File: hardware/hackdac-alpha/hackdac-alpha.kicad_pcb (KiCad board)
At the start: 4 copper layers, 120 x 75 mm, 222 parts, among them J1 VIDEO OUT, J10 HOLE, J11 HOLE, J12 EXT POWER, J13 TTL SYNC, J2 SYNC OUT, J3 I2C, J4 AUDIO OUT, J5 EXT 5V, J6 HOLE, J7 HOLE, J8 HOLE, J9 HOLE, P1 BANK2_AUX, P2 P22, P3 P20, P4 P28, Q1 2N7002, Q2 BC857, Q3 BC857, Q4 2N7002, Q5 2N7002, Q6 IRLML2244, U1 AD768, U10 KF50BDT, U11 L78L05_SO8, U12 L79L05_SO8, U13 LM66200, U14 TPS61170DRVR, U15 TPS63700DRCT, U2 MAX4104, U3 TLE2082, U4 MAX4104, U5 MCP47FEB22A1-E/ST, U6 74LVCH16T245, U7 74LVC1T45, U8 MCP1700T-3302E/MB, U9 PCM5102, X1 ECS-TXO-3225-270-TR

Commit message: Update with V2 mods
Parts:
- added REF**: SOT-23, Package_TO_SOT_SMD:SOT-23, F.Cu at (137.1, 107.7)
- added REF**: R_0603_1608Metric, Resistor_SMD:R_0603_1608Metric, F.Cu at (146.0, 118.3)
- added REF**: R_0603_1608Metric, Resistor_SMD:R_0603_1608Metric, F.Cu at (134.9, 108.9)
- added U16: 74LVC1G125, Package_TO_SOT_SMD:SOT-23-5, F.Cu at (148.2, 120.8)
- L11: value L -> 5u6
- R21: value 1k8 -> 750
- R24: value 270 -> 487
- R36: value 1k8 -> 1k5
- R53, R54: value R -> 100
- R57: value NF -> 0
- R60: value 55k6 -> 30k9
- R63: value 988k -> 619k
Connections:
- P2 pad 2: unconnected-(P2-Pin_2-Pad2) -> TCXO_CLK
- P4 pad 15: TCXO_CLK -> unconnected-(P4-Pin_15-Pad15)
- P4 pad 3: unconnected-(P4-Pin_3-Pad3) -> TCXO_ENABLE
- R32 pad 2: TCXO_CLK -> Net-(R32-Pad2)
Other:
- board text added: "REWORK WIRE LENGTHS: TCXO_CLK: 51MM U16 IN: 19MM GND: 9MM"

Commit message: V3 PCB WIP
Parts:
- removed the C54 at (158.4, 79.8)
- removed the C68 at (183.3, 82.5)
- removed the C69 at (160.7, 93.7)
- removed the C71 at (183.3, 86.6)
- removed the C72 at (151.8, 96.1)
- removed the C73 at (151.8, 99.9)
- removed the C74 at (137.4, 94.8)
- removed the C75 at (137.4, 100.0)
- removed C79: 100n, Capacitor_SMD:C_0603_1608Metric
- removed the D5 at (182.5, 77.5)
- removed the J5 at (185.9, 75.8)
- removed the L11 at (123.6, 126.9)
- removed the L12 at (164.8, 96.5)
- removed the L13 at (164.8, 100.0)
- removed L16: NF, Inductor_SMD:L_1210_3225Metric
- removed L17: 5u6, Inductor_SMD:L_1210_3225Metric
- removed the R45 at (108.8, 129.9)
- removed the R46 at (108.8, 131.6)
- removed the R47 at (108.8, 133.2)
- removed the R48 at (108.8, 134.9)
- removed the R55 at (157.5, 95.7)
- removed the R56 at (157.5, 102.3)
- removed the R57 at (182.8, 94.4)
- removed REF**: SOT-23, Package_TO_SOT_SMD:SOT-23
- removed REF** (x2): R_0603_1608Metric, Resistor_SMD:R_0603_1608Metric
- removed the U11 at (157.5, 97.6)
- removed the U12 at (157.5, 103.3)
- removed U13: LM66200, Package_TO_SOT_SMD:SOT-583-8
- removed U16: 74LVC1G125, Package_TO_SOT_SMD:SOT-23-5
- added D7: RF OUT, LED_SMD:LED_0805_2012Metric, F.Cu at (220.7, 78.9)
- added J6: EXT LEDS, Connector_Molex:Molex_PicoBlade_53047-0410_1x04_P1.25mm_Vertical, F.Cu at (233.3, 77.3)
- added Q2: BC847, Package_TO_SOT_SMD:SOT-23, F.Cu at (208.9, 79.8)
- added R50: 100, Resistor_SMD:R_0603_1608Metric, F.Cu at (220.5, 81.7)
- added R51: 100, Resistor_SMD:R_0603_1608Metric, F.Cu at (228.7, 78.0)
- added R52: 100, Resistor_SMD:R_0603_1608Metric, F.Cu at (228.7, 80.5)
- added R54: 10k, Resistor_SMD:R_0603_1608Metric, F.Cu at (228.7, 83.1)
- C10: value 1n -> 1n5
- C11: value 560p -> NF
- C12, C17, C18, C29: value 100p -> NF
- C13: value 82p -> NF
- C14: value 100p -> 270p
- C15: value 680p -> 3n9
- C16: value 2n2 -> NF
- C19: value 100p -> 300p
- C20: value 1n -> NF
- C21: renamed from C22; value 82p -> 300p
- C22: renamed from C21; value 220p -> NF
- C24: renamed from C25; value 220p -> 620p
- C25: renamed from C24; value 390p -> NF
- C26: renamed from C27; value 270p -> NF
- C27: renamed from C26; value NF -> 270p
- C28: value 560p -> 680p
- C30: value 18p -> NF
- C31: value 220p -> 240p
- C36: value 47p -> 47pF
- C40: renamed from C41; value 560p -> 1n
- C41: renamed from C40; value 390p -> NF
- R13, R20: value 100 -> NF
- R14, R18: value 100 -> 50
- R21: value 750 -> 470
- R22: renamed from R23; value 180 -> 169
- R23: renamed from R22; value 3k3 -> NF
- R24: value 487 -> 330
- R25: value 330 -> 220
- R26: value 100 -> 75
- R32: renamed from R39; value 100 -> 39
- R33: value 10 -> 10k
- R34: renamed from R31; value NF -> 10k
- R36: renamed from R32; value 100 -> 39
- R49: value 0 -> 100
- U10: value KF50BDT -> 74LVC1G07; footprint Package_TO_SOT_SMD:TO-252-2 -> Package_TO_SOT_SMD:SOT-23-5
- U7: value 74LVC1T45 -> 74LVC1G125; footprint Package_TO_SOT_SMD:SOT-23-6 -> Package_TO_SOT_SMD:SOT-23-5
- moved R49 130.9 mm to (228.7, 75.5), turned to 0 degrees
- moved R33 93.6 mm to (228.7, 87.6), turned to 0 degrees
- moved Q1 82.2 mm to (208.9, 84.4), turned to 0 degrees
- moved C70 52.3 mm to (121.2, 71.4)
- moved C48 36.4 mm to (168.8, 109.3), turned to -90 degrees
- moved U7 32.9 mm to (165.8, 109.2), turned to 0 degrees
- moved C69 29.1 mm to (130.0, 65.3), turned to 0 degrees
- moved C65 19.3 mm to (148.9, 96.8), turned to -90 degrees
- moved C66 17.9 mm to (150.6, 96.8)
- moved R36 15.8 mm to (162.8, 109.3), turned to -90 degrees
- moved U10 14.5 mm to (181.2, 95.2)
- moved X1 11.8 mm to (159.7, 109.2), turned to 90 degrees
- moved C47 11.4 mm to (156.7, 109.3), turned to -90 degrees
- moved L12 11.4 mm to (137.2, 98.4)
- moved L11 11.3 mm to (137.2, 95.0)
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- renumbered C46 to C45, C47 to C46, C45 to C47, C55 to C54, C56 to C55, C57 to C56, C58 to C57, C59 to C58, C60 to C59, C61 to C60, C62 to C61, C63 to C62, C64 to C63, C65 to C64, C66 to C65, C67 to C66, C76 to C67, C77 to C68, C78 to C69, C80 to C71, C81 to C72, C82 to C73, C83 to C74, C84 to C75, C85 to C76, C86 to C77, C87 to C78, D6 to D5, D7 to D6, J8 to J10, J9 to J11, J10 to J12, J11 to J13, J13 to J2, J2 to J3, J3 to J4, J4 to J5, J12 to J7, J6 to J8, J7 to J9, L14 to L11, L15 to L12, L18 to L13, L19 to L14, P4 to P3, P3 to P4, Q2 to Q3, Q3 to Q4, Q4 to Q5, Q5 to Q6, Q6 to Q7, R35 to R31, R34 to R35, R36 to R37, R37 to R38, R38 to R39, R50 to R45, R51 to R46, R52 to R47, R53 to R48, R54 to R53, R58 to R55, R59 to R56, R60 to R57, R61 to R58, R62 to R59, R63 to R60, U14 to U11, U15 to U12
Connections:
- C45 pad 1: VCC -> +5V
- C46 pad 1: VCC -> +5V
- C53 pad 2: -VDAC -> -5VA
- C54 pad 1: Net-(U8-VI) -> VIN
- C63 pad 1: Net-(J4-IN2) -> Net-(J5-IN2)
- C64 pad 1: Net-(J4-IN1) -> Net-(J5-IN1)
- C65 pad 1: +VDAC -> +5V
- C66 pad 2: -VDAC -> -5V
- C70 pad 2: Net-(C70-Pad2) -> -5VA
- C76 pad 1: +VDAC -> +5V
- C77 pad 1: -VDAC -> -5V
- D4 pad 1: -VDAC -> -5VA
- D5 pad 1: GND -> Net-(D5-K)
- D5 pad 2: Net-(D6-A) -> +3.3V_HACKRF
- D6 pad 1: Net-(D7-K) -> Net-(D6-K)
- D8 pad 1: +VDAC -> +5V
- D9 pad 2: -VDAC -> -5V
- J5 pad 1: Net-(J4-IN1) -> Net-(J5-IN1)
- J5 pad 2: Net-(J4-IN2) -> Net-(J5-IN2)
- J7 pad 1: +VDAC -> -5V
- J7 pad 3: -VDAC -> +5V
- P1 pad 17: /video-misc/LAD0 -> unconnected-(P1-Pin_17-Pad17)
- P2 pad 22: unconnected-(P2-Pin_22-Pad22) -> PWR_EN
- P3 pad 7: unconnected-(P4-Pin_7-Pad7) (its old number) -> /power/RF_OUT_LED
- P4 pad 13: unconnected-(P3-Pin_13-Pad13) (its old number) -> GND
- P4 pad 15: unconnected-(P3-Pin_15-Pad15) (its old number) -> GND
- P4 pad 17: /power/VBUSCTRL -> unconnected-(P4-Pin_17-Pad17)
- P4 pad 19: unconnected-(P3-Pin_19-Pad19) (its old number) -> GND
- Q1 pad 1: Net-(Q1-G) -> LSYNC
- Q3 pad 2: Net-(Q1-D) -> Net-(Q2-C)
- Q4 pad 3: -VDAC -> -5VA
- Q7 pad 1: /power/VBUSCTRL -> Net-(Q7-G)
- Q7 pad 3: Net-(Q6-D) -> VIN
- R31 pad 2: Net-(U7-A) -> Net-(U6-1A1)
- R32 pad 1: Net-(U7-B) -> Net-(U6-1B1)
- R33 pad 1: LSYNC -> +5VA
- R33 pad 2: Net-(Q1-G) -> Net-(Q1-D)
- R35 pad 2: Net-(Q1-D) -> Net-(Q2-C)
- R36 pad 2: Net-(R32-Pad2) -> Net-(R36-Pad2)
- R46 pad 2: Net-(J4-IN1) -> Net-(J5-IN2)
- R47 pad 2: Net-(J4-IN2) -> Net-(J5-IN1)
- R48 pad 1: +3.3V_HACKRF -> Net-(D5-K)
- R48 pad 2: Net-(D6-A) -> GND
- R49 pad 2: Net-(U9-SCK) -> Net-(J6-Pin_2)
- R53 pad 1: /power/VIDEO_OUT_LED -> /power/RF_OUT_LED
- R57 pad 1: +VDAC -> +5V
- R60 pad 2: -VDAC -> -5V
- U1 pad 7: AD0 -> GND
- U10 pad 1: Net-(D5-K) -> (no net)
- U10 pad 2: GND -> PWR_EN
- U10 pad 3: Net-(U10-VO) -> GND
- U12 pad 8: -VDAC -> -5V
- U6 pad 18: VCC -> +5V
- U6 pad 2: AD0 -> Net-(U6-1B1)
- U6 pad 47: /video-misc/LAD0 -> Net-(U6-1A1)
- U6 pad 7: VCC -> +5V
- U7 pad 1: +3.3V_HACKRF -> TCXO_ENABLE
- U7 pad 2: GND -> Net-(R36-Pad2)
- U7 pad 3: Net-(U7-A) -> GND
- U7 pad 4: Net-(U7-B) -> TCXO_CLK
- U8 pad 2: Net-(U8-VI) -> VIN
- U9 pad 12: Net-(U9-SCK) -> GND
- U9 pad 13: Net-(U9-BCK) -> /audio/I2S_SCK
- U9 pad 14: Net-(U9-DIN) -> /audio/I2S_SDA
- U9 pad 15: Net-(U9-LRCK) -> /audio/I2S_WS
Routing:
- net GND: track 1209.2 -> 1031.0 mm, vias 174 -> 133
- net -VDAC: track 106.5 -> 0.00 mm, vias 12 -> 0
- net +VDAC: track 60.6 -> 0.00 mm, vias 12 -> 0
- net (no net): track 0.00 -> 57.1 mm
- net PWR_EN: track 0.00 -> 45.0 mm, vias 0 -> 1
- net VCC: track 44.0 -> 0.00 mm, vias 6 -> 0
- net Net-(J4-IN2): track 37.4 -> 0.00 mm
- net AD0: track 32.4 -> 0.00 mm, vias 2 -> 0
- net TCXO_CLK: track 10.5 -> 40.8 mm, vias 0 -> 1
- net +3.3V_HACKRF: track 250.9 -> 279.1 mm, vias 11 -> 8
- net TCXO_ENABLE: track 0.00 -> 27.4 mm, vias 0 -> 1
- net Net-(U8-VI): track 22.7 -> 0.00 mm, vias 11 -> 0
- net VIN: track 157.7 -> 136.8 mm, vias 13 -> 14
- net Net-(J4-IN1): track 18.0 -> 0.00 mm
- net Net-(C70-Pad2): track 18.0 -> 0.00 mm
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- added copper zone on In1.Cu, net +5V
- added copper zone on F.Cu, net -5V
- removed copper zone on F.Cu, net +VDAC
- removed copper zone on In1.Cu, net +VDAC
- removed copper zone on F.Cu, net -VDAC
- removed copper zone on In1.Cu, net -VDAC
- removed copper zone on F.Cu, net Net-(Q6-D)
- removed copper zone on F.Cu, net Net-(U10-VO)
- removed copper zone on In1.Cu, net Net-(U8-VI)
- removed copper zone on In1.Cu, net VCC
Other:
- board text added: "HackDAC Alpha v3"
- board text removed: "+12V IN"
- board text removed: "HackDAC Alpha v2"
- board text removed: "REWORK WIRE LENGTHS: TCXO_CLK: 51MM U16 IN: 19MM GND: 9MM"

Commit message: V3 PCB WIP
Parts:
- moved D7 126.6 mm to (100.0, 116.9), turned to 180 degrees
- moved R49 121.4 mm to (103.5, 114.1), turned to 180 degrees
- moved R33 92.8 mm to (137.5, 104.6)
- moved J6 86.9 mm to (149.9, 101.7)
- moved Q2 83.9 mm to (131.8, 113.1)
- moved Q1 75.8 mm to (137.2, 108.9)
- moved R53 45.6 mm to (184.0, 91.5)
- moved R48 5.34 mm to (103.5, 111.4), turned to 0 degrees
- moved D5 5.33 mm to (100.0, 111.4), turned to 180 degrees
- moved C63 5.25 mm to (94.6, 126.7)
- moved C64 5.16 mm to (94.6, 131.9)
- moved R50 2.80 mm to (103.5, 116.9)
- turned D6 to 180 degrees
- renumbered R50 to R49, R53 to R50, R49 to R51, R51 to R52, R54 to R53, R52 to R54
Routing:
- net (no net): track 57.1 -> 0.00 mm
- net /power/RF_OUT_LED: track 0.00 -> 47.8 mm
- net Net-(J5-IN2): track 0.00 -> 33.1 mm
- net Net-(J5-IN1): track 0.00 -> 21.9 mm
- net GND: track 1031.0 -> 1020.2 mm
- net +3.3V_HACKRF: track 279.1 -> 284.4 mm
- net Net-(D7-K): track 6.07 -> 1.73 mm
- net Net-(D5-K): track 0.00 -> 1.98 mm
- net Net-(D6-K): track 0.00 -> 1.73 mm
- net /power/VIDEO_OUT_LED: track 50.8 -> 52.1 mm
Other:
- board text added: "SERIAL NUMBER:"

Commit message: V3 layout mostly complete
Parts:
- JP2, JP3: footprint Jumper:SolderJumper-3_P1.3mm_Open_Pad1.0x1.5mm -> Jumper:SolderJumper-3_P1.3mm_Bridged12_Pad1.0x1.5mm
- moved R51 83.5 mm to (150.0, 103.4)
- moved R52 82.2 mm to (150.0, 101.8)
- moved R54 81.1 mm to (150.0, 100.1)
- moved J6 7.69 mm to (157.4, 100.1), turned to 180 degrees
- moved C54 4.29 mm to (122.0, 126.9), turned to 90 degrees
- moved C49 2.57 mm to (133.3, 109.7), turned to -90 degrees
- moved J7 2.54 mm to (162.6, 101.7)
- moved R33 1.65 mm to (137.4, 106.2)
- moved R35 1.42 mm to (131.5, 109.7)
- moved R53 1.31 mm to (183.1, 92.5)
- moved C55 0.64 mm to (114.9, 126.9)
- moved C48 0.51 mm to (169.4, 109.3)
- moved R34 0.51 mm to (155.5, 109.3)
- moved R36 0.51 mm to (163.3, 109.3)
- moved U7 0.51 mm to (166.3, 109.2)
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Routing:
- net GND: track 1020.2 -> 1056.7 mm, vias 133 -> 136
- net -5V: track 35.9 -> 66.1 mm
- net -5VA: track 104.9 -> 127.6 mm, vias 12 -> 14
- net /power/VIDEO_OUT_LED: track 52.1 -> 69.1 mm
- net +5V: track 152.1 -> 167.0 mm, vias 14 -> 15
- net /power/RF_OUT_LED: track 47.8 -> 62.1 mm
- net Net-(Q1-D): track 0.00 -> 10.5 mm
- net VIN: track 136.8 -> 144.8 mm, vias 14 -> 16
- net Net-(J6-Pin_2): track 0.00 -> 7.52 mm
- net +3.3V_HACKRF: track 284.4 -> 291.9 mm, vias 8 -> 11
- net Net-(Q7-G): track 4.19 -> 9.84 mm
- net Net-(J6-Pin_3): track 0.00 -> 5.00 mm
- net /power/VBUS: track 7.69 -> 11.7 mm
- net Net-(J6-Pin_4): track 0.00 -> 2.83 mm
- net +5VA: track 134.4 -> 137.0 mm, vias 14 -> 13
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
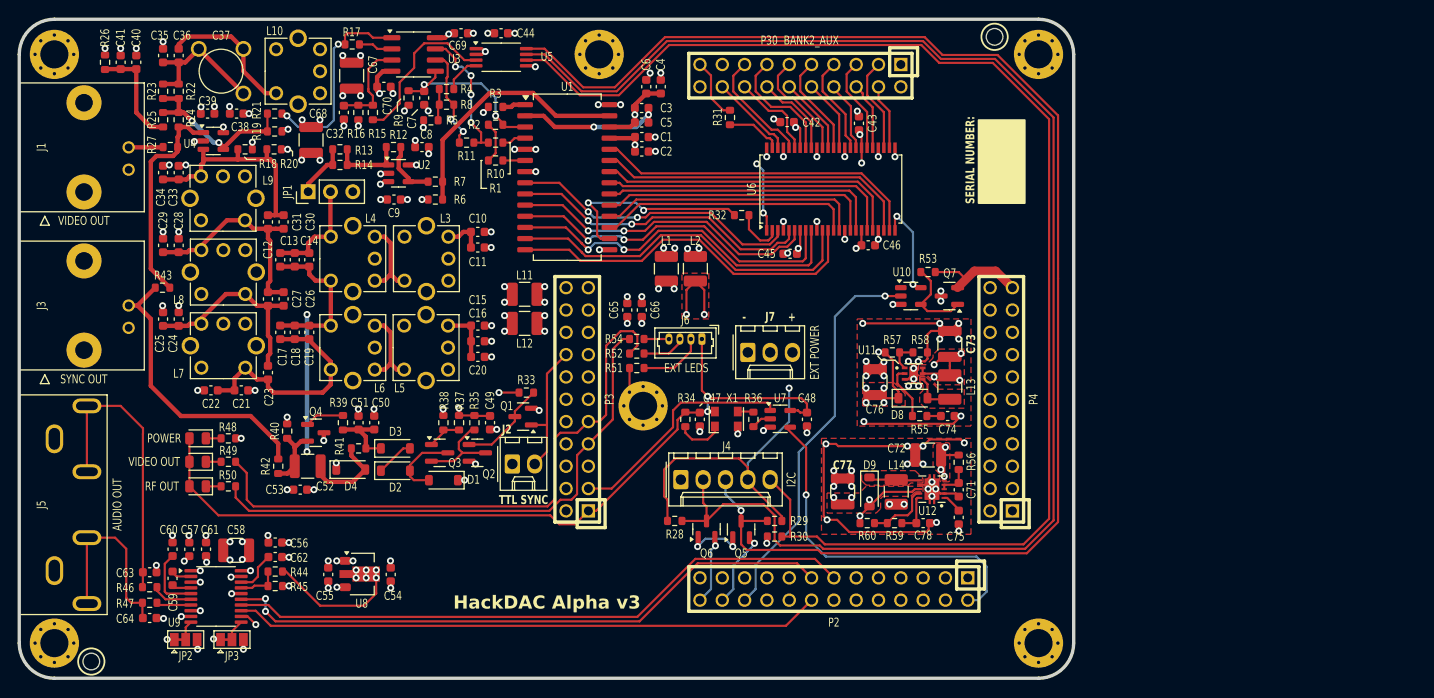
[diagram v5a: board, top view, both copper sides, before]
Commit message: Optional caps for DAC supply
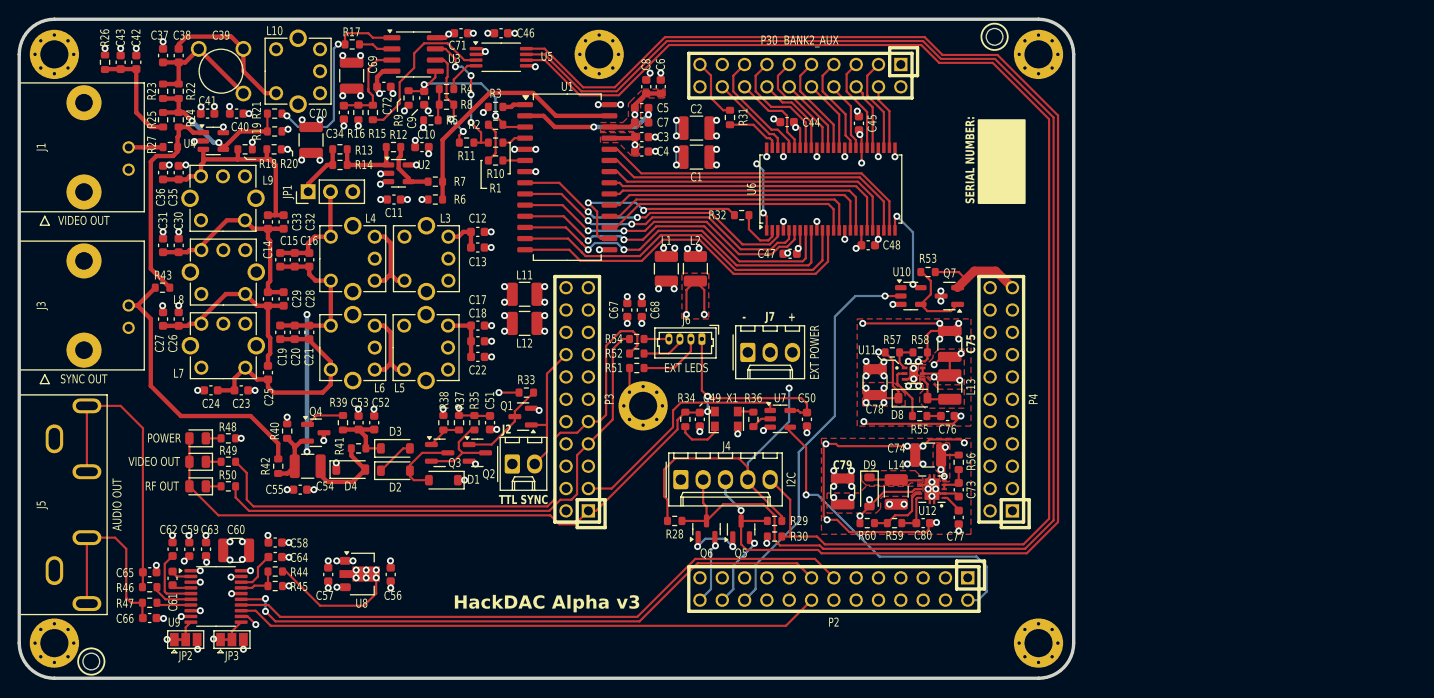
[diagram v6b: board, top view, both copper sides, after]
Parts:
- added C1: 33u, Capacitor_SMD:C_1210_3225Metric, F.Cu at (156.8, 79.4)
- added C2: 33u, Capacitor_SMD:C_1210_3225Metric, F.Cu at (156.8, 76.1)
- renumbered C8 to C10, C9 to C11, C10 to C12, C11 to C13, C12 to C14, C13 to C15, C14 to C16, C15 to C17, C16 to C18, C17 to C19, C18 to C20, C19 to C21, C20 to C22, C21 to C23, C22 to C24, C23 to C25, C24 to C26, C25 to C27, C26 to C28, C27 to C29, C1 to C3, C28 to C30, C29 to C31, C30 to C32, C31 to C33, C32 to C34, C33 to C35, C34 to C36, C35 to C37, C36 to C38, C37 to C39, C2 to C4, C38 to C40, C39 to C41, C40 to C42, C41 to C43, C42 to C44, C43 to C45, C44 to C46, C45 to C47, C46 to C48, C47 to C49, C3 to C5, C48 to C50, C49 to C51, C50 to C52, C51 to C53, C52 to C54, C53 to C55, C54 to C56, C55 to C57, C56 to C58, C57 to C59, C4 to C6, C58 to C60, C59 to C61, C60 to C62, C61 to C63, C62 to C64, C63 to C65, C64 to C66, C65 to C67, C66 to C68, C67 to C69, C5 to C7, C68 to C70, C69 to C71, C70 to C72, C71 to C73, C72 to C74, C73 to C75, C74 to C76, C75 to C77, C76 to C78, C77 to C79, C6 to C8, C78 to C80, C7 to C9
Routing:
- net GND: track 1056.7 -> 1068.2 mm, vias 136 -> 140
- net /video/ADAC-: track 31.7 -> 38.1 mm, vias 3 -> 5
- net /video/ADAC+: track 22.3 -> 28.0 mm, vias 3 -> 5
- net TCXO_CLK: track 40.8 -> 38.0 mm
- added copper zone on F.Cu, net /video/ADAC+
- added copper zone on F.Cu, net /video/ADAC-
